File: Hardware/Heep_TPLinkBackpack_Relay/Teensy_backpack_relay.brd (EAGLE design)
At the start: 45 x 57.5 mm, 37 parts, among them Q2 600mA/40V, U1 ENC28J60-SSOP

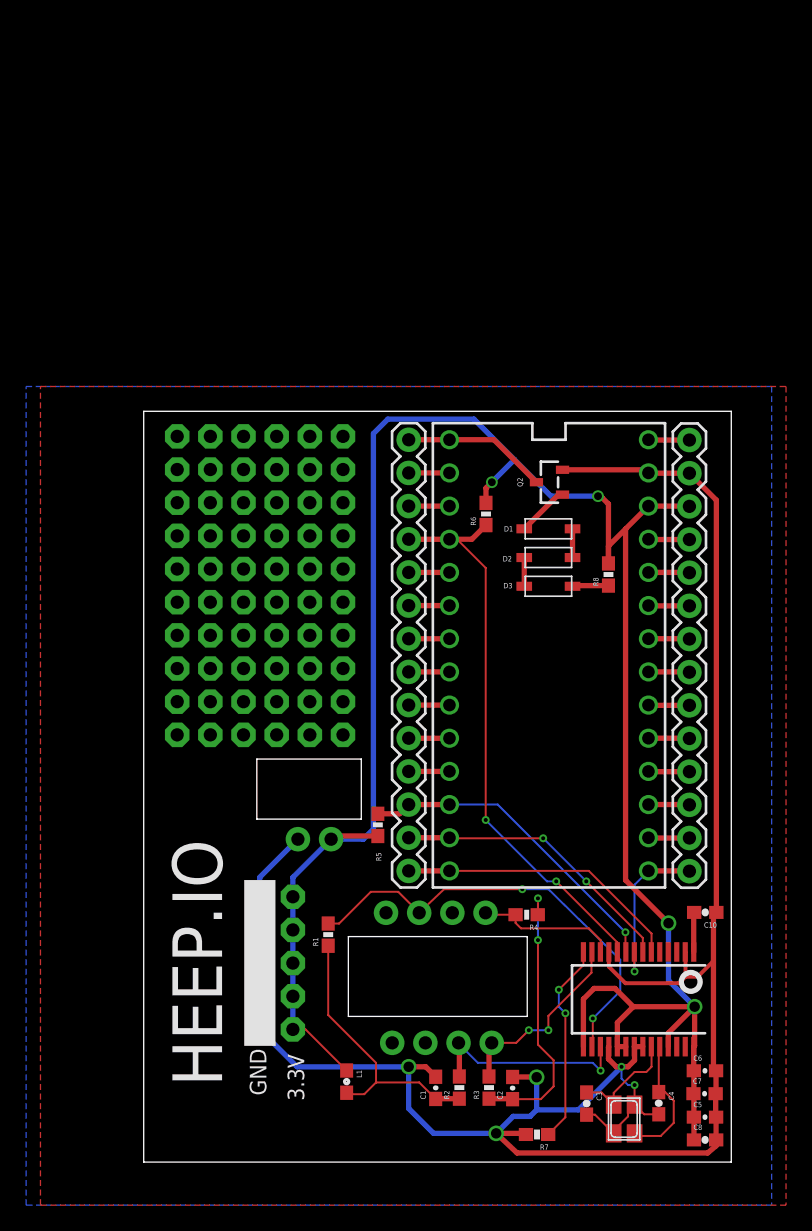
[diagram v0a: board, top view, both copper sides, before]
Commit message: #44 Finalized TPLink Backpack Schematics and Layouts
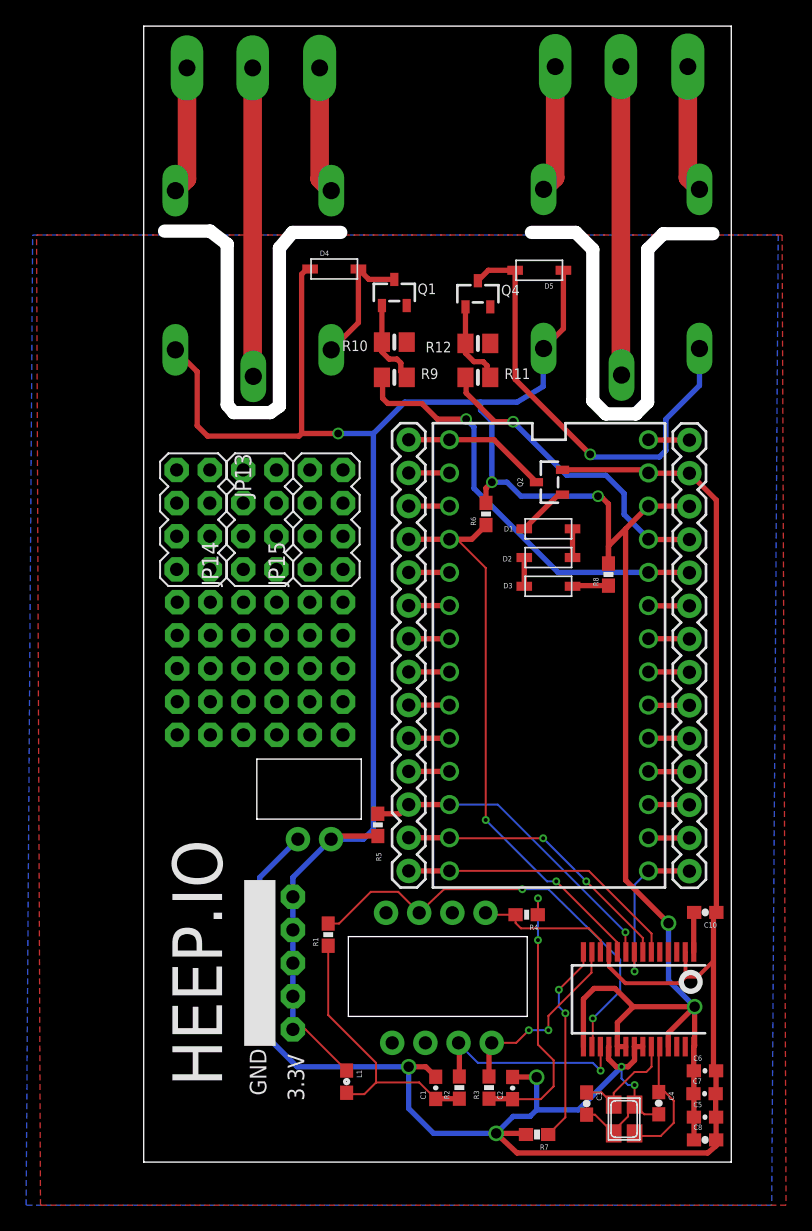
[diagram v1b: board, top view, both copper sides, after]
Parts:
- removed JP3, JP5, JP7: (no value), SparkFun-Connectors:2X5_NOSILK
- added D4, D5: 200mA/100V/1V, adafruit:SOD-123
- added JP11, JP12: (no value), microbuilder:TERMBLOCK_1X3_5.08MM
- added JP13, JP14, JP15: (no value), SparkFun-Connectors:2X4
- added K1, K2: G5LE, relay:G5LE
- added Q1, Q4: MMBT2222, microbuilder:SOT23-R
- added R10, R12: 10K, microbuilder:0805-NO
- added R11, R9: 1K, microbuilder:0805-NO
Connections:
- removed net N$20: BREAKOUT1.4, U$1.23/A9
- removed net N$21: BREAKOUT1.5, U$1.22/A8
- new net N$30: D5.A, K2.2, Q4.3
- new net N$31: JP11.1, K1.S
- new net N$32: JP11.3, K1.O
- new net N$33: JP11.2, K1.P
- new net N$34: Q1.1, R10.2, R9.2
- new net N$35: JP12.1, K2.S
- new net N$36: JP12.3, K2.O
- new net N$37: JP12.2, K2.P
- new net N$38: D4.A, K1.2, Q1.3
- new net N$39: Q4.1, R11.2, R12.2
- new net RELAY_L: BREAKOUT1.5, R9.1, U$1.22/A8
- new net RELAY_R: BREAKOUT1.4, R11.1, U$1.23/A9
- net 3.3V: now also D4.C, D5.C, K1.1, K2.1
- net AGND: now also Q1.2, Q4.2, R10.1, R12.1
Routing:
- net 3.3V: track 167.7 -> 217.5 mm, vias 4 -> 5
- net N$30: track 0.00 -> 34.6 mm, vias 0 -> 1
- net RELAY_L: track 0.00 -> 33.4 mm, vias 0 -> 1
- net RELAY_R: track 0.00 -> 23.9 mm, vias 0 -> 1
- net N$37: track 0.00 -> 23.6 mm
- net N$33: track 0.00 -> 23.6 mm
- net N$38: track 0.00 -> 10.1 mm
- net N$36: track 0.00 -> 9.77 mm
- net N$35: track 0.00 -> 9.77 mm
- net N$31: track 0.00 -> 9.77 mm
- net N$32: track 0.00 -> 9.77 mm
- net N$34: track 0.00 -> 6.64 mm
- net N$39: track 0.00 -> 6.60 mm
- net N$21: track 3.15 -> 0.00 mm
- net N$20: track 3.15 -> 0.00 mm
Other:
- board size 45 x 57.5 mm -> 45 x 87 mm
